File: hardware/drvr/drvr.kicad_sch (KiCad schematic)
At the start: 25 parts, among them J101 PinHeader2x2, J102 PinHeader2x2, J103 PinHeader2x2, J104 PinHeader2x2, J105 PinHeader2x2, J106 PinHeader2x2, J107 pwrCon_Solder_5mm, J108 pwrCon_Solder_5mm, J109 pwrCon_Solder_5mm, J110 pwrCon_Solder_5mm, J111 pwrCon_Solder_5mm, J112 pwrCon_Solder_5mm, J113 pwrCon_Solder_5mm

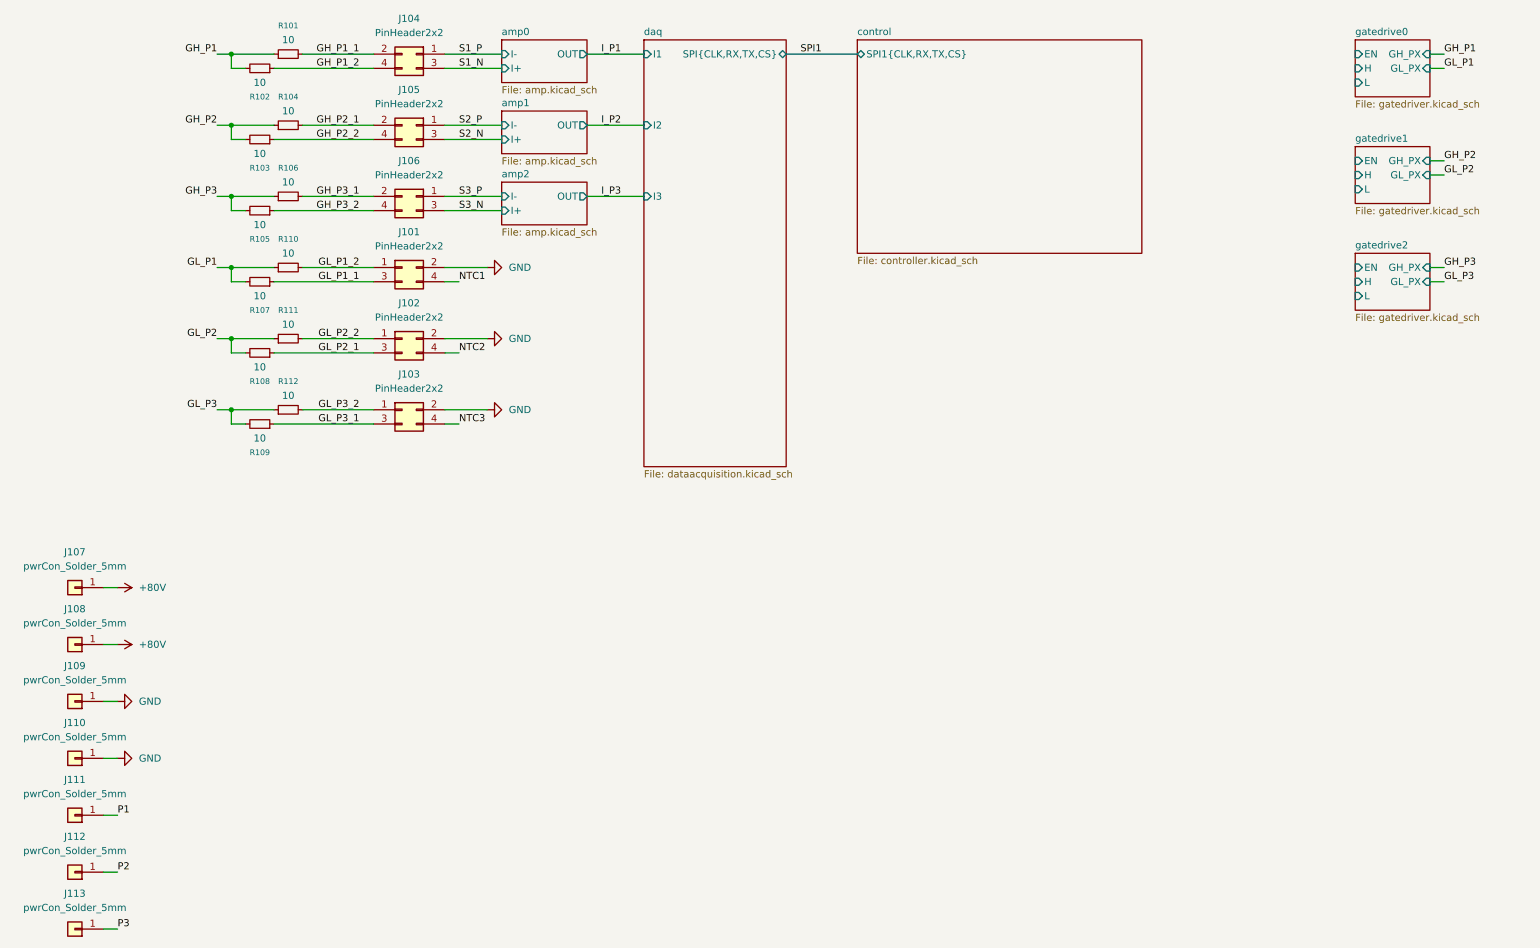
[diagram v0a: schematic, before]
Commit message: added gatedrivers + pico as draft
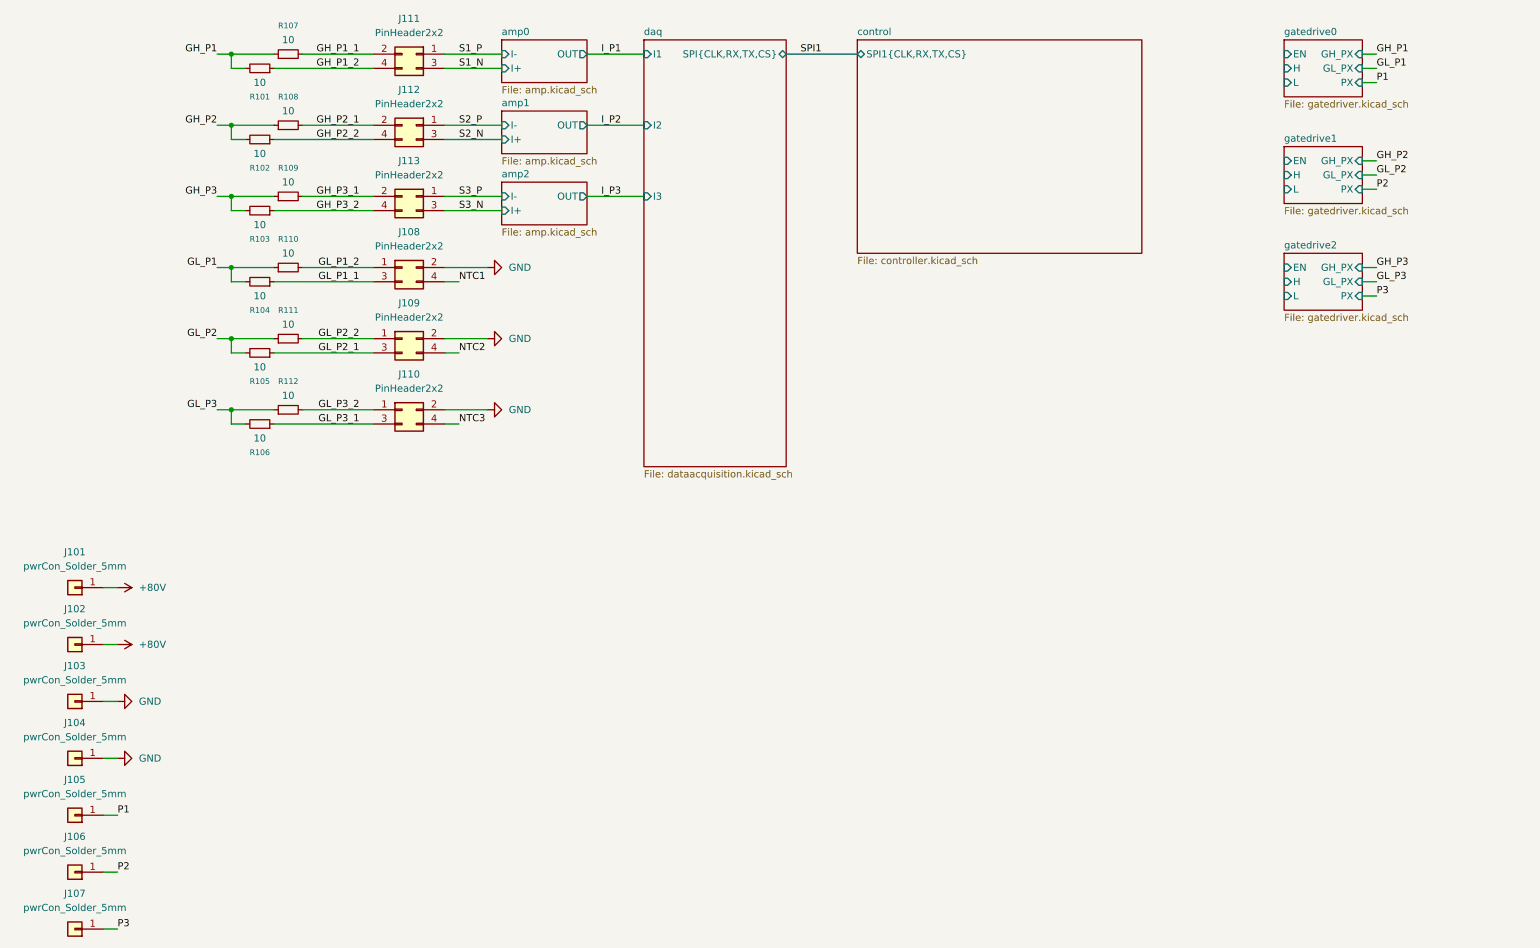
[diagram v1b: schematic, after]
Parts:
- renumbered J107 to J101, J108 to J102, J109 to J103, J110 to J104, J111 to J105, J112 to J106, J113 to J107, J101 to J108, J102 to J109, J103 to J110, J104 to J111, J105 to J112, J106 to J113, R102 to R101, R103 to R102, R105 to R103, R107 to R104, R108 to R105, R109 to R106, R101 to R107, R104 to R108, R106 to R109
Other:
- sheet gatedrive0 ports: added PX; removed none
- sheet gatedrive1 ports: added PX; removed none
- sheet gatedrive2 ports: added PX; removed none
